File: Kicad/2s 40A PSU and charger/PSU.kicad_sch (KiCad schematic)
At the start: 10 parts, among them U2 AP63203WU, U7 TPS7A2633DRV

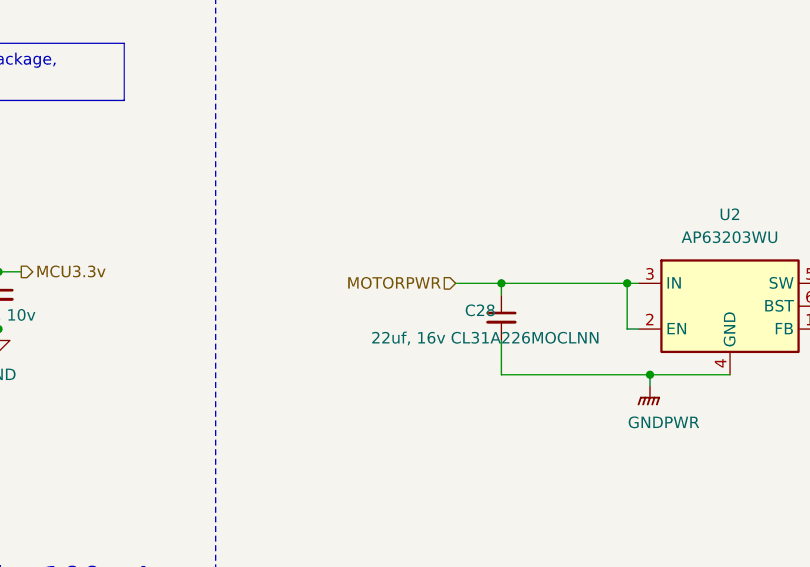
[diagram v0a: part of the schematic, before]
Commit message: Updated 3v3 psu traces and capacitor position
I rotated the input capacitor to make a more compact shape, and I played around with some of the trace thicknesses
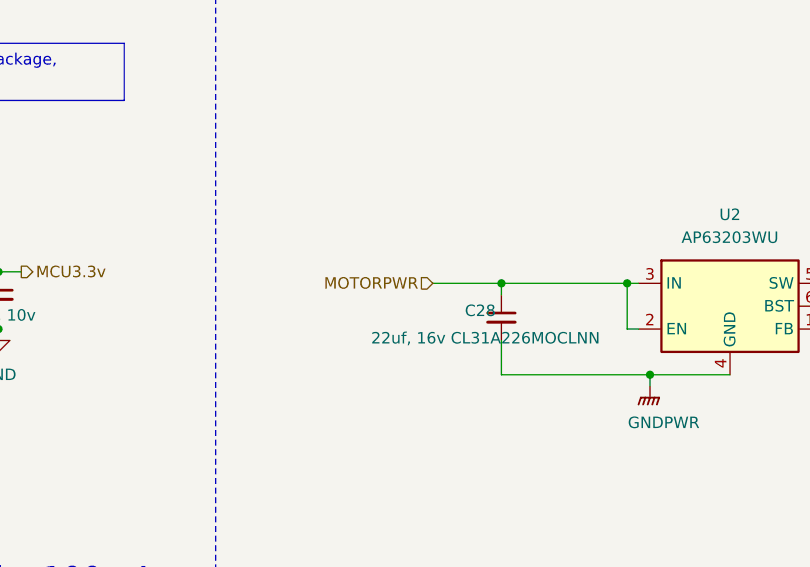
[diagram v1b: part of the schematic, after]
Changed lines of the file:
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@@
-	(wire
-		(pts
-			(xy 173.99 76.2) (xy 179.07 76.2)
-		)
-		(stroke
-			(width 0)
-			(type default)
-		)
-	)
 	(wire
 		(pts
@@
 		(pts
 			(xy 99.06 72.39) (xy 107.95 72.39)
+		)
+		(stroke
+			(width 0)
+			(type default)
+		)
+	)
+	(wire
+		(pts
+			(xy 171.45 76.2) (xy 179.07 76.2)
 		)
 		(stroke
@@
 	(hierarchical_label "MOTORPWR"
 		(shape input)
-		(at 173.99 76.2 180)
+		(at 171.45 76.2 180)
 		(fields_autoplaced yes)
 		(effects
@@
 		)
 	)
+	(netclass_flag ""
+		(length 2.54)
+		(shape round)
+		(at 184.15 76.2 0)
+		(effects
+			(font
+				(size 1.27 1.27)
+			)
+			(justify left bottom)
+		)
+		(property "Netclass" "Charge Current"
+			(at 178.816 69.85 0)
+			(effects
+				(font
+					(size 1.27 1.27)
+					(italic yes)
+				)
+				(justify left)
+			)
+		)
+	)

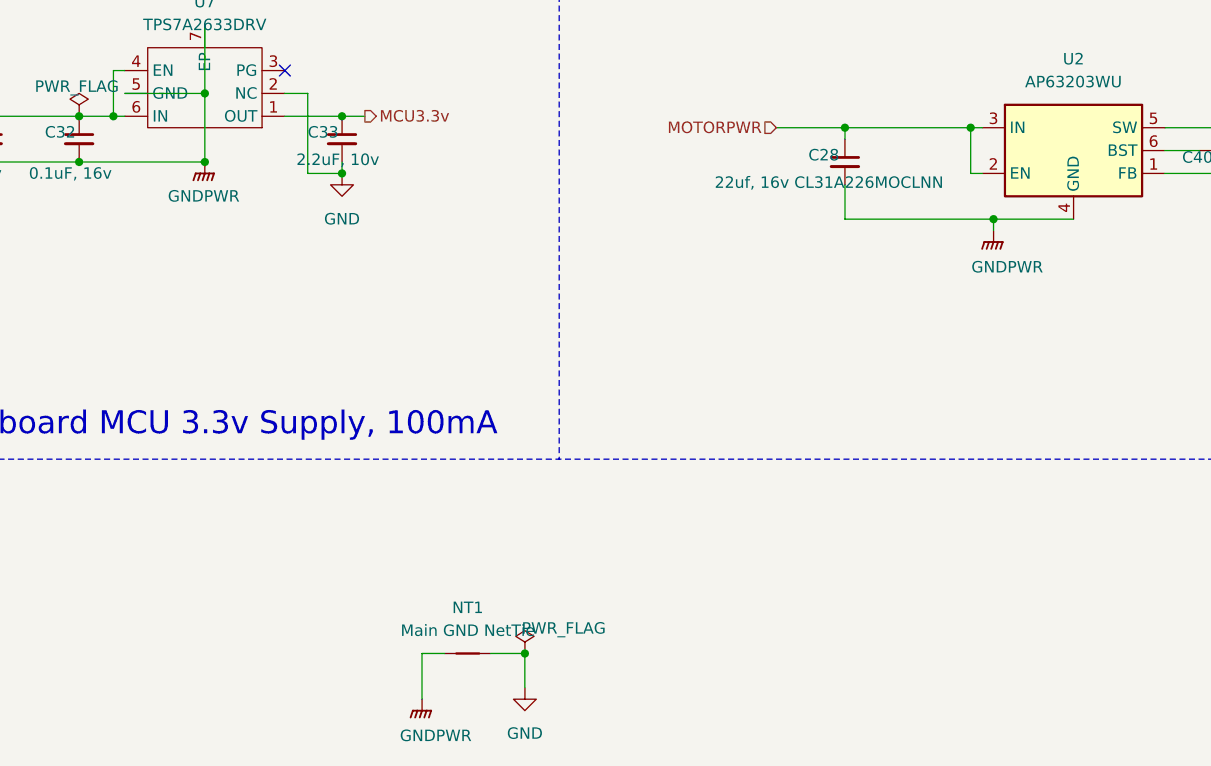
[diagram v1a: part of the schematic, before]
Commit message: Combined separate ground planes
I now have one solid ground plane. There really was no point in having separate ground planes EXCEPT for keeping the high current return path away from the MCU and sense lines. I have added a keepout zone on the top half, to split to keep the high current return from going into the MCU section, but that is it.
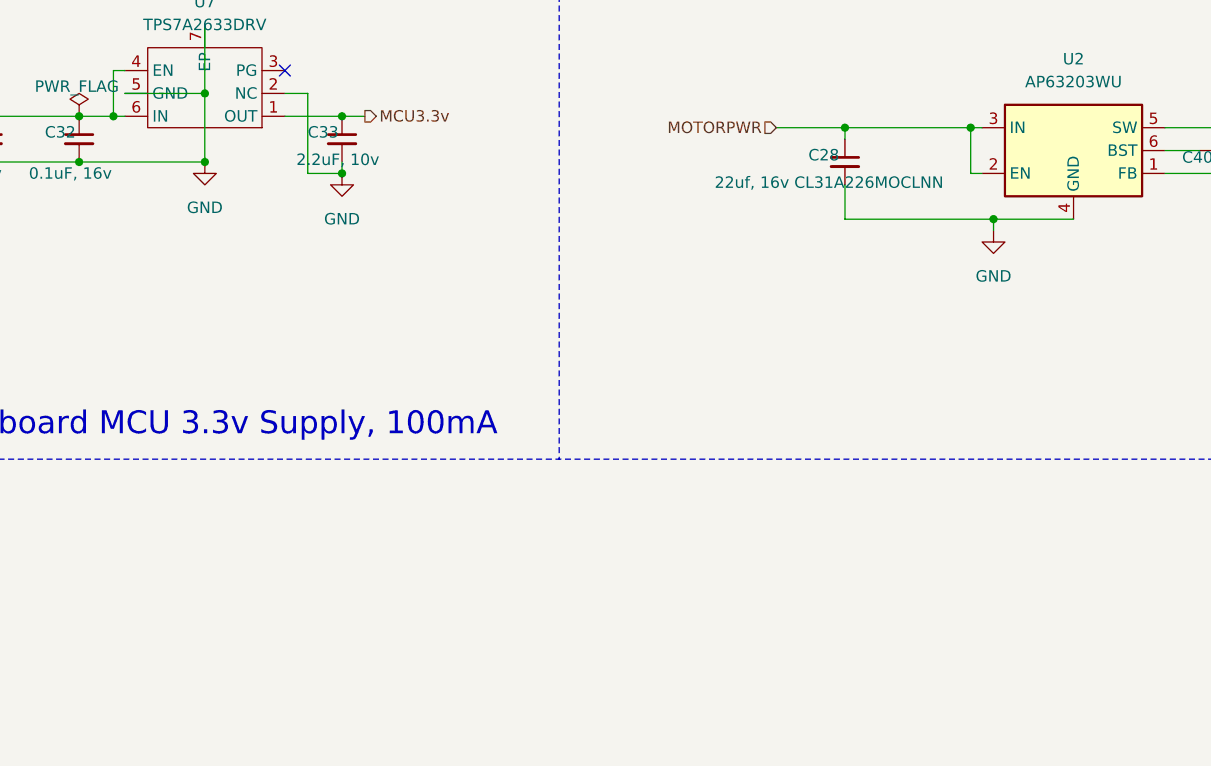
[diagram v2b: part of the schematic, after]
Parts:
- removed NT1: Main GND NetTie, NetTie:NetTie-2_SMD_Pad2.0mm, symbol Device:NetTie_2
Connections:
- net GNDPWR is gone; now on net GND: C28.2, C31.2, C32.2, U2.4 (GND), U7.5 (GND), U7.7 (EP)

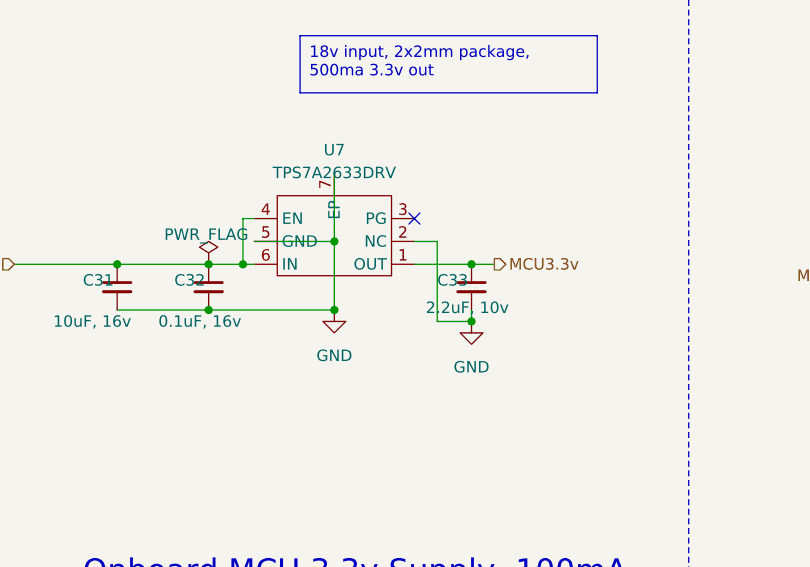
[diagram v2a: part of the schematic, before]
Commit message: Final tweaks, capacitor placement and GND keepouts
I tried my best to isolate signal grounds from the power paths. I also added a bunch of ground keepouts to help isolate.
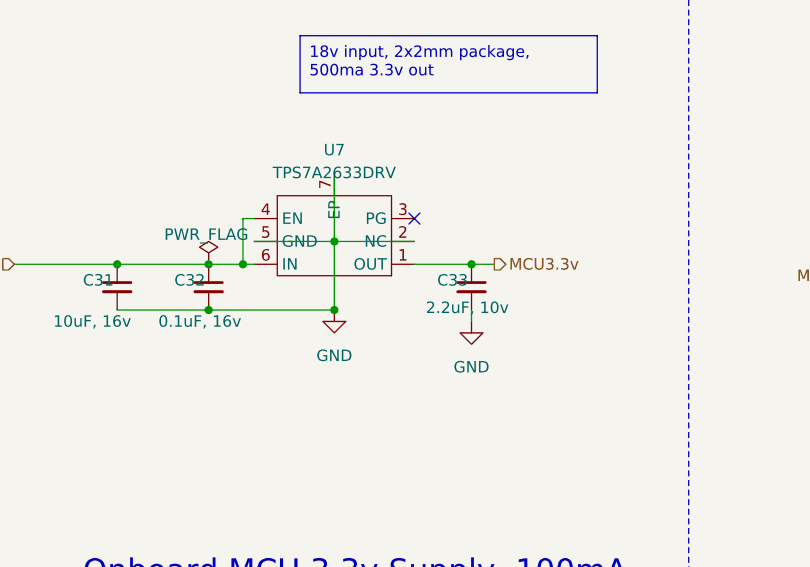
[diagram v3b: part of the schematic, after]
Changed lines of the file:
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@@
 	(title_block
 		(title "CACKLE 2s 40A PSU & Charger")
-		(date "2024-12-01")
+		(date "2024-12-23")
 		(rev "V1")
 		(comment 1 "Author: Asher Edwards")
@@
 	)
 	(junction
-		(at 123.19 81.28)
-		(diameter 0)
-		(color 0 0 0 0)
-	)
-	(junction
 		(at 236.22 76.2)
 		(diameter 0)
@@
 	(wire
 		(pts
+			(xy 107.95 72.39) (xy 116.84 72.39)
+		)
+		(stroke
+			(width 0)
+			(type default)
+		)
+	)
+	(wire
+		(pts
 			(xy 72.39 74.93) (xy 83.82 74.93)
 		)
@@
 	(wire
 		(pts
-			(xy 116.84 72.39) (xy 119.38 72.39)
-		)
-		(stroke
-			(width 0)
-			(type default)
-		)
-	)
-	(wire
-		(pts
 			(xy 195.58 87.63) (xy 195.58 86.36)
 		)
@@
 	(wire
 		(pts
-			(xy 119.38 72.39) (xy 119.38 81.28)
-		)
-		(stroke
-			(width 0)
-			(type default)
-		)
-	)
-	(wire
-		(pts
 			(xy 236.22 81.28) (xy 236.22 76.2)
 		)
@@
 		)
 		(stroke
-			(width 0)
-			(type default)
-		)
-	)
-	(wire
-		(pts
-			(xy 119.38 81.28) (xy 123.19 81.28)
-		)
-		(stroke

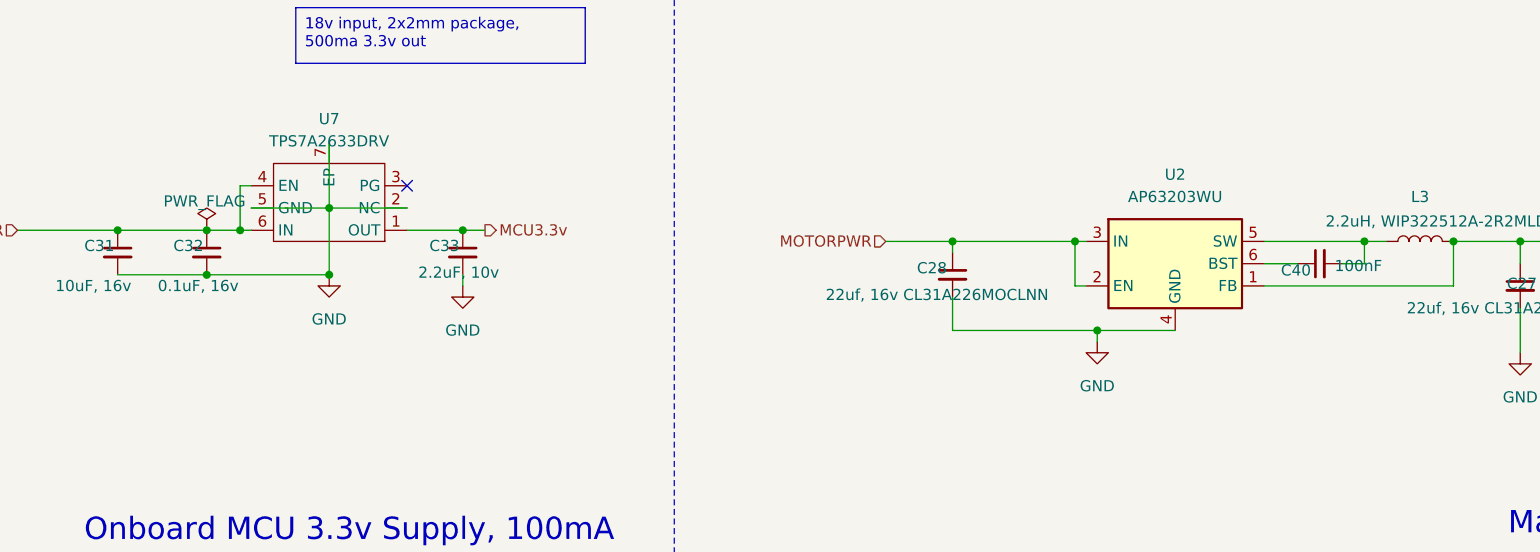
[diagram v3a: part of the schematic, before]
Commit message: Added LCSC part numbers, DNP attr, and exported Gerbers
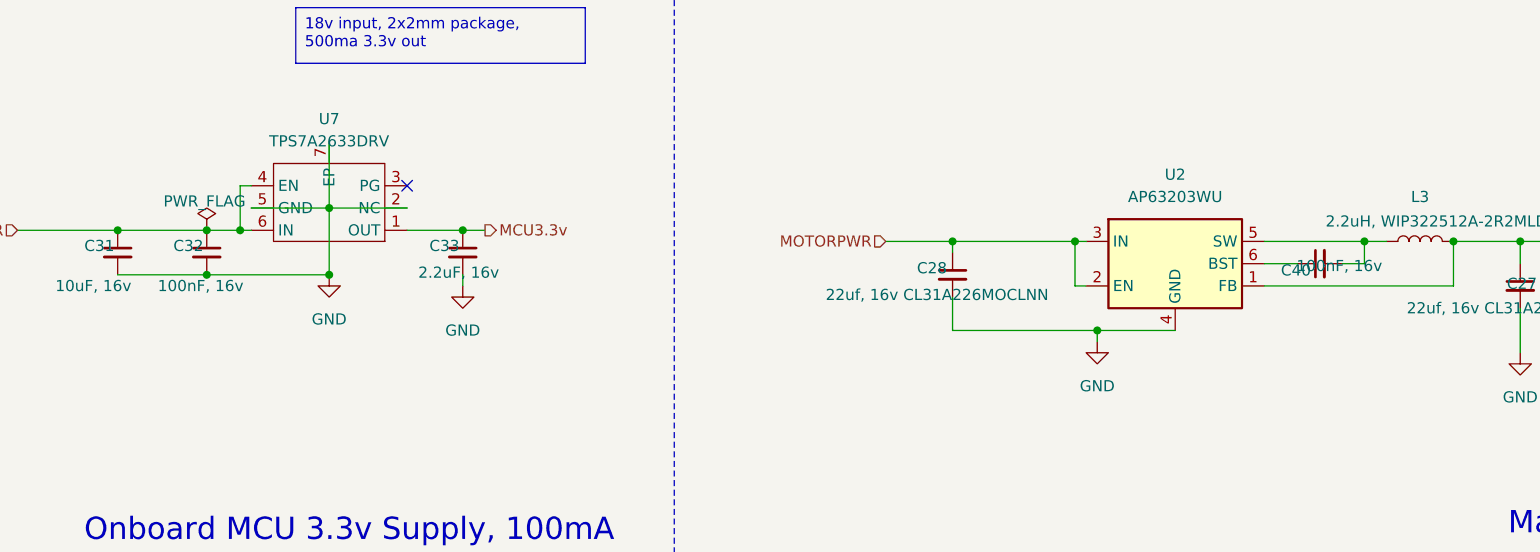
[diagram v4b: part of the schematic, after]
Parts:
- C27, C28: LCSC (none) -> C159758
- C31: LCSC (none) -> C96446
- C32: value 0.1uF, 16v -> 100nF, 16v; LCSC (none) -> C1525
- C33: value 2.2uF, 10v -> 2.2uF, 16v; LCSC (none) -> C12530
- C40: value 100nF -> 100nF, 16v; LCSC (none) -> C14663
- L3: LCSC (none) -> C5832372
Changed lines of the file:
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@@
+			)
+		)
+		(property "LCSC" "C5832372"
+			(at 232.41 76.2 90)
+			(effects
+				(font
+					(size 1.27 1.27)
+				)
+				(hide yes)
 			)
 		)
@@
 			)
 		)
-		(property "Value" "0.1uF, 16v"
+		(property "Value" "100nF, 16v"
 			(at 88.392 81.28 0)
 			(effects
@@
 			)
 		)
+		(property "LCSC" "C1525"
+			(at 90.17 76.708 0)
+			(effects
+				(font
+					(size 1.27 1.27)
+				)
+				(hide yes)
+			)
+		)
 		(pin "1"
 		)
@@
 			)
 		)
+		(property "LCSC" "C96446"
+			(at 80.01 76.708 0)
+			(effects
+				(font
+					(size 1.27 1.27)
+				)
+				(hide yes)
+			)
+		)
 		(pin "1"
 		)
@@
 			)
 		)
-		(property "Value" "2.2uF, 10v"
+		(property "Value" "2.2uF, 16v"
 			(at 118.11 79.756 0)
 			(effects
@@
 		(property "Description" "Unpolarized capacitor, small symbol"
 			(at 123.19 77.47 0)
+			(effects
+				(font
+					(size 1.27 1.27)
+				)
+				(hide yes)
+			)
+		)
+		(property "LCSC" "C12530"
+			(at 119.38 76.708 0)
 			(effects
 				(font
@@
 			)
 		)
-		(property "Value" "100nF"
+		(property "Value" "100nF, 16v"
 			(at 228.092 78.994 90)
 			(effects
@@
 			)
 		)
+		(property "LCSC" "C14663"
+			(at 219.964 79.502 0)
+			(effects
+				(font
+					(size 1.27 1.27)
+				)
+				(hide yes)
+			)
+		)
 		(pin "1"
 		)
@@
 		(property "Description" "Unpolarized capacitor, small symbol"
 			(at 179.07 80.01 0)
+			(effects
+				(font
+					(size 1.27 1.27)
+				)
+				(hide yes)
+			)
+		)
+		(property "LCSC" "C159758"
+			(at 175.006 79.248 0)
 			(effects
 				(font
@@
 			(effects
 				(font
+					(size 1.27 1.27)
+				)
+				(hide yes)
+			)
+		)
+		(property "LCSC" "C159758"
+			(at 242.316 81.026 0)
+			(effects
+				(font
